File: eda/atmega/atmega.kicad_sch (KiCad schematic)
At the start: 8 parts, among them SW1 Push_Button, U1 ATmega328P-P, Y1 Crystal_16MHz

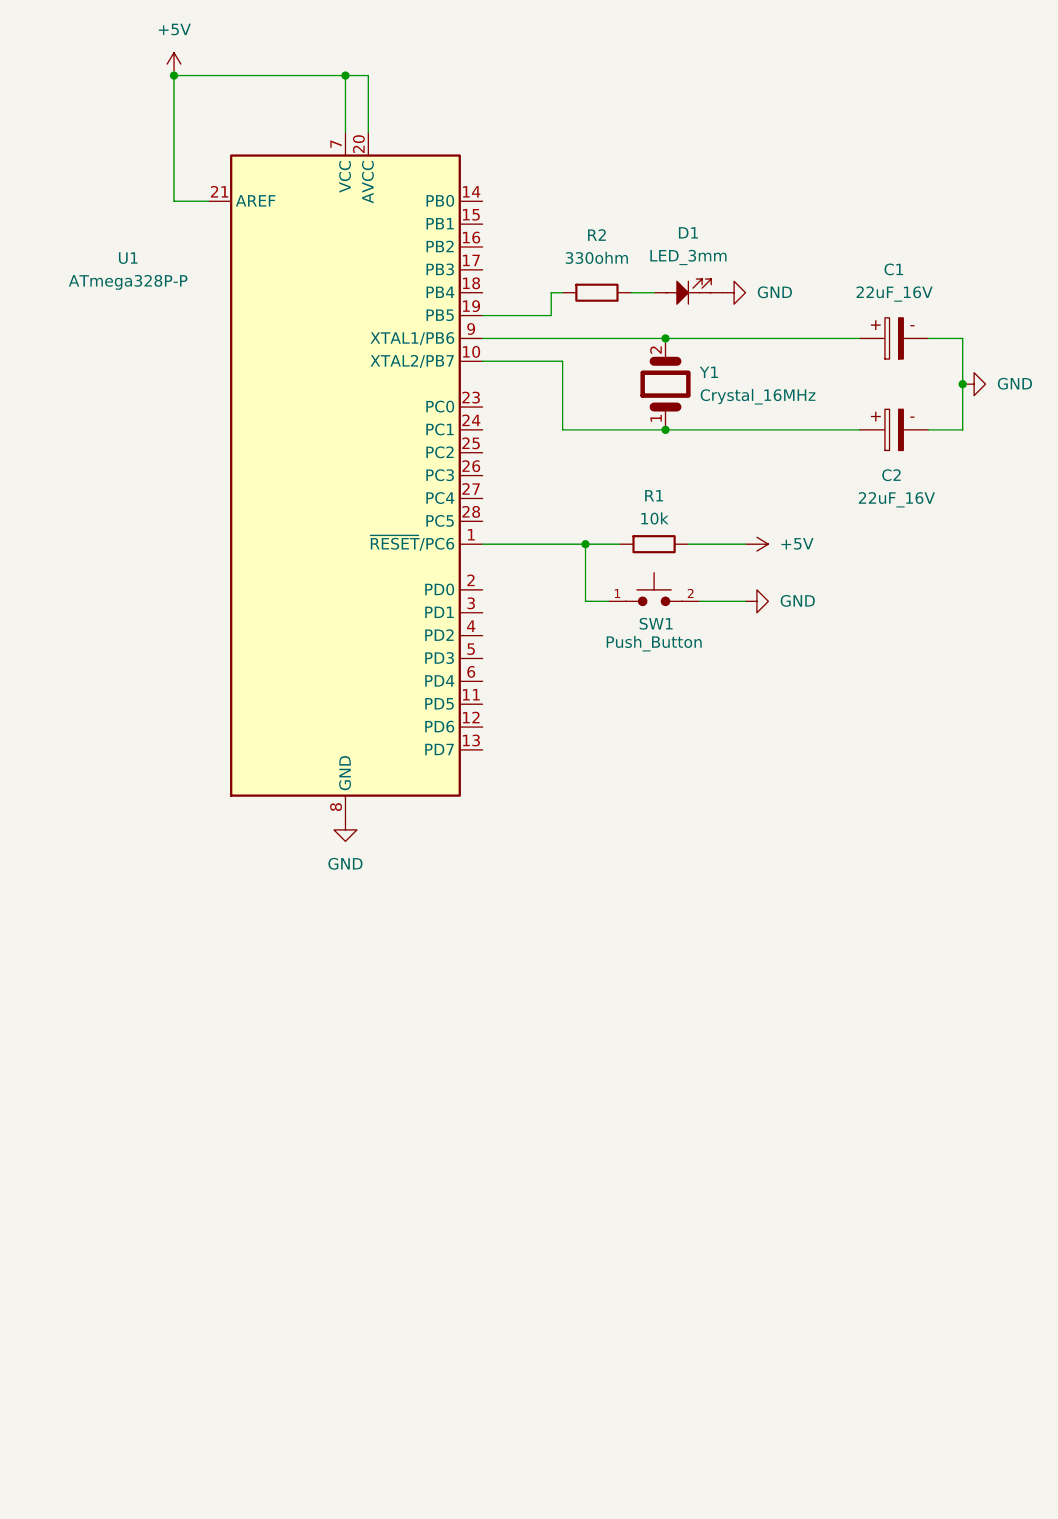
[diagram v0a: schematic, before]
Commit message: Add bootloader circuit
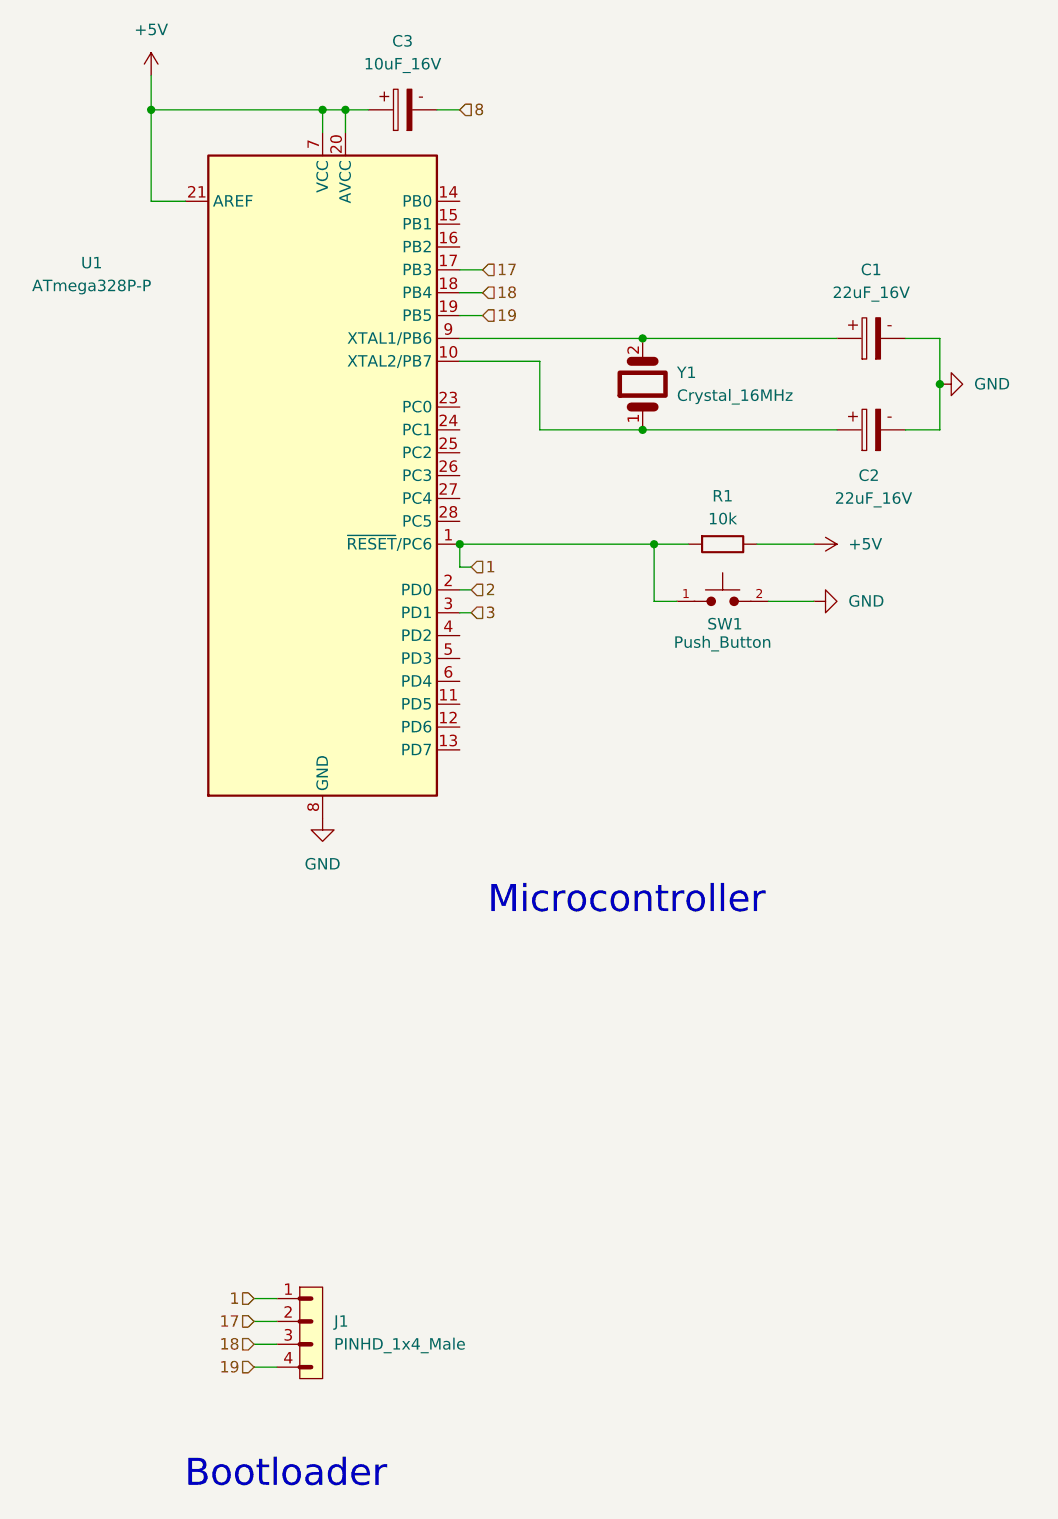
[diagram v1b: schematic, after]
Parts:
- removed D1: LED_3mm, LED_THT:LED_D3.0mm, symbol PCM_SL_Devices:LED_3mm
- removed R2: 330ohm, Resistor_THT:R_Axial_DIN0207_L6.3mm_D2.5mm_P10.16mm_Horizontal, symbol PCM_SL_Resistors:330ohm
- added C3: 10uF_16V, Capacitor_THT:CP_Radial_D5.0mm_P2.00mm, symbol PCM_SL_Capacitors:10uF_16V
- added J1: PINHD_1x4_Male, Connector_PinHeader_2.54mm:PinHeader_1x04_P2.54mm_Vertical, symbol PCM_SL_Pin_Headers:PINHD_1x4_Male
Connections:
- net +5V: now also C3.1
- net 1: now reaches R1.1, SW1.1, U1.1 (~{RESET}/PC6)
- net 1: now also J1.1
- net 17: now reaches U1.17 (PB3)
- net 17: now also J1.2
- net 18: now reaches U1.18 (PB4)
- net 18: now also J1.3
- net 19: now reaches U1.19 (PB5)
- net 19: now also J1.4
- net 2: now reaches U1.2 (PD0)
- net 3: now reaches U1.3 (PD1)
- new net 8: C3.2
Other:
- note added: "Bootloader"
- note added: "Microcontroller"
- moved on the sheet: C1, C2, R1, SW1, U1, Y1
